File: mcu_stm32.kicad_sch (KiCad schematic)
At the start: 1 part, among them U1 STM32F103C6Tx

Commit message: stm32 added
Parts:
- removed U1: STM32F103C6Tx, Package_QFP:LQFP-48_7x7mm_P0.5mm, symbol MCU_ST_STM32F1:STM32F103C6Tx
- added C27, C28, C29, C30, C35: 0.1u, Capacitor_SMD:C_0805_2012Metric, symbol Device:C_Small
- added C31, C32, C33, C34: 20p, Capacitor_SMD:C_0805_2012Metric, symbol Device:C_Small
- added C36: 1uf, Capacitor_SMD:C_0805_2012Metric, symbol Device:C_Small
- added J16: Debug, Connector_PinHeader_2.54mm:PinHeader_1x04_P2.54mm_Vertical, symbol PCM_SL_Pin_Headers:PINHD_1x4_Male
- added J17: Boot_Sel, Connector_PinHeader_2.54mm:PinHeader_2x03_P2.54mm_Vertical, symbol PCM_SL_Pin_Headers:PINHD_2x3_Male
- added P1: USB_C_Plug_USB2.0, symbol Connector:USB_C_Plug_USB2.0
- added R16: 1M, Resistor_SMD:R_0805_2012Metric, symbol Device:R_Small
- added R17: 10K, Resistor_SMD:R_0805_2012Metric, symbol Device:R_Small
- added R18, R19: 100K, Resistor_SMD:R_0805_2012Metric, symbol Device:R_Small
- added R20, R21: 20R, Resistor_SMD:R_0805_2012Metric, symbol Device:R_Small
- added R22: 4.7K, Resistor_SMD:R_0805_2012Metric, symbol Device:R_Small
- added SW1: RESET, Button_Switch_SMD:SW_SPST_CK_KMS2xxGP, symbol Switch:SW_Push
- added U7: STM32F103C8Tx, Package_QFP:LQFP-48_7x7mm_P0.5mm, symbol MCU_ST_STM32F1:STM32F103C8Tx
- added Y1: 8mHz, symbol Device:Crystal_Small
- added Y2: 32.768kHz, symbol Device:Crystal_GND24_Small
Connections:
- new net: J17.3, R18.2
- new net: P1.A6 (D+), R21.1
- new net: J17.4, R19.1
- new net: P1.A7 (D-), R20.1
- new net 3V3: C27.2, C28.2, C29.2, C30.2, C35.2, J16.4, J17.1, J17.2, R17.1, U7.24 (VDD), U7.36 (VDD), U7.48 (VDD), U7.9 (VDDA)
- new net 5V1: P1.A4 (VBUS), P1.A9 (VBUS), P1.B4 (VBUS), P1.B9 (VBUS), R22.1
- new net BOOT0: R18.1, U7.44 (BOOT0)
- new net BOOT1: R19.2, U7.19 (PB1)
- new net GND: C27.1, C28.1, C29.1, C30.1, C31.2, C32.2, C33.2, C34.1, C35.1, C36.1, J16.1, J17.5, J17.6, P1.A1 (GND), P1.A12 (GND), P1.B1 (GND), P1.B12 (GND), P1.S1 (SHIELD), SW1.1, U7.23 (VSS), U7.35 (VSS), U7.47 (VSS), U7.8 (VSSA), Y2.2, Y2.4
- new net OSC_IN: C31.1, R16.1, U7.5 (PD0), Y1.2
- new net OSC_OUT: C32.1, R16.2, U7.6 (PD1), Y1.1
- new net PC14: C33.1, U7.3 (PC14), Y2.1
- new net PC15: C34.2, U7.4 (PC15), Y2.3
- new net RESET: C36.2, R17.2, SW1.2, U7.7 (NRST)
- new net SWCLK: J16.2
- new net SWDIO: J16.3
- new net USB_D+: R21.2, R22.2, U7.33 (PA12)
- new net USB_D-: R20.2, U7.32 (PA11)
- no-connect marks 0 -> 3

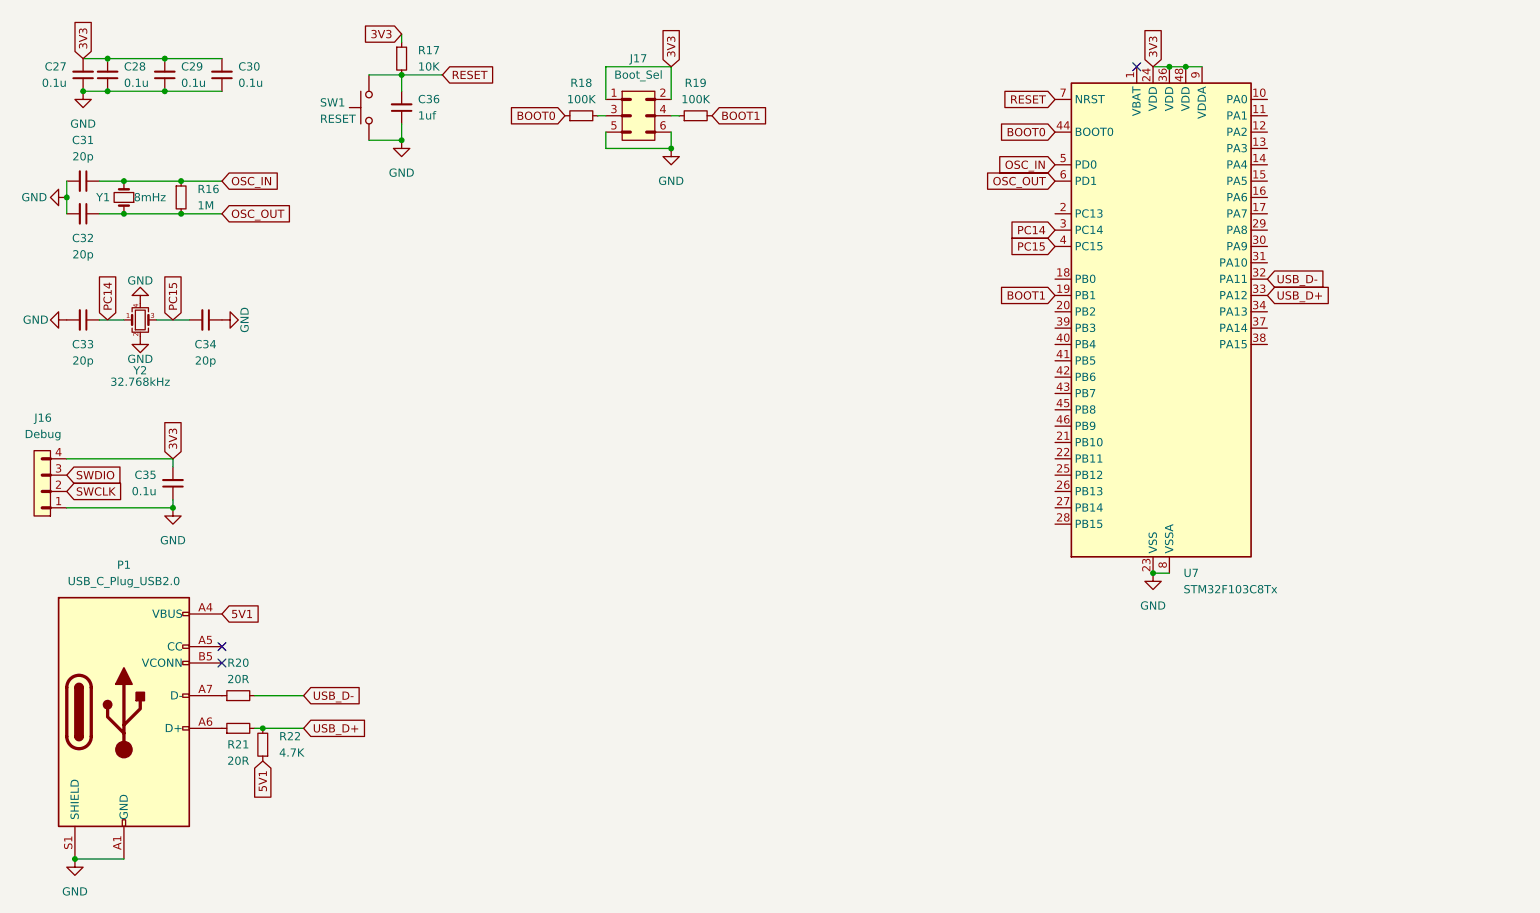
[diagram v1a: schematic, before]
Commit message: added components
servo controller, esp32
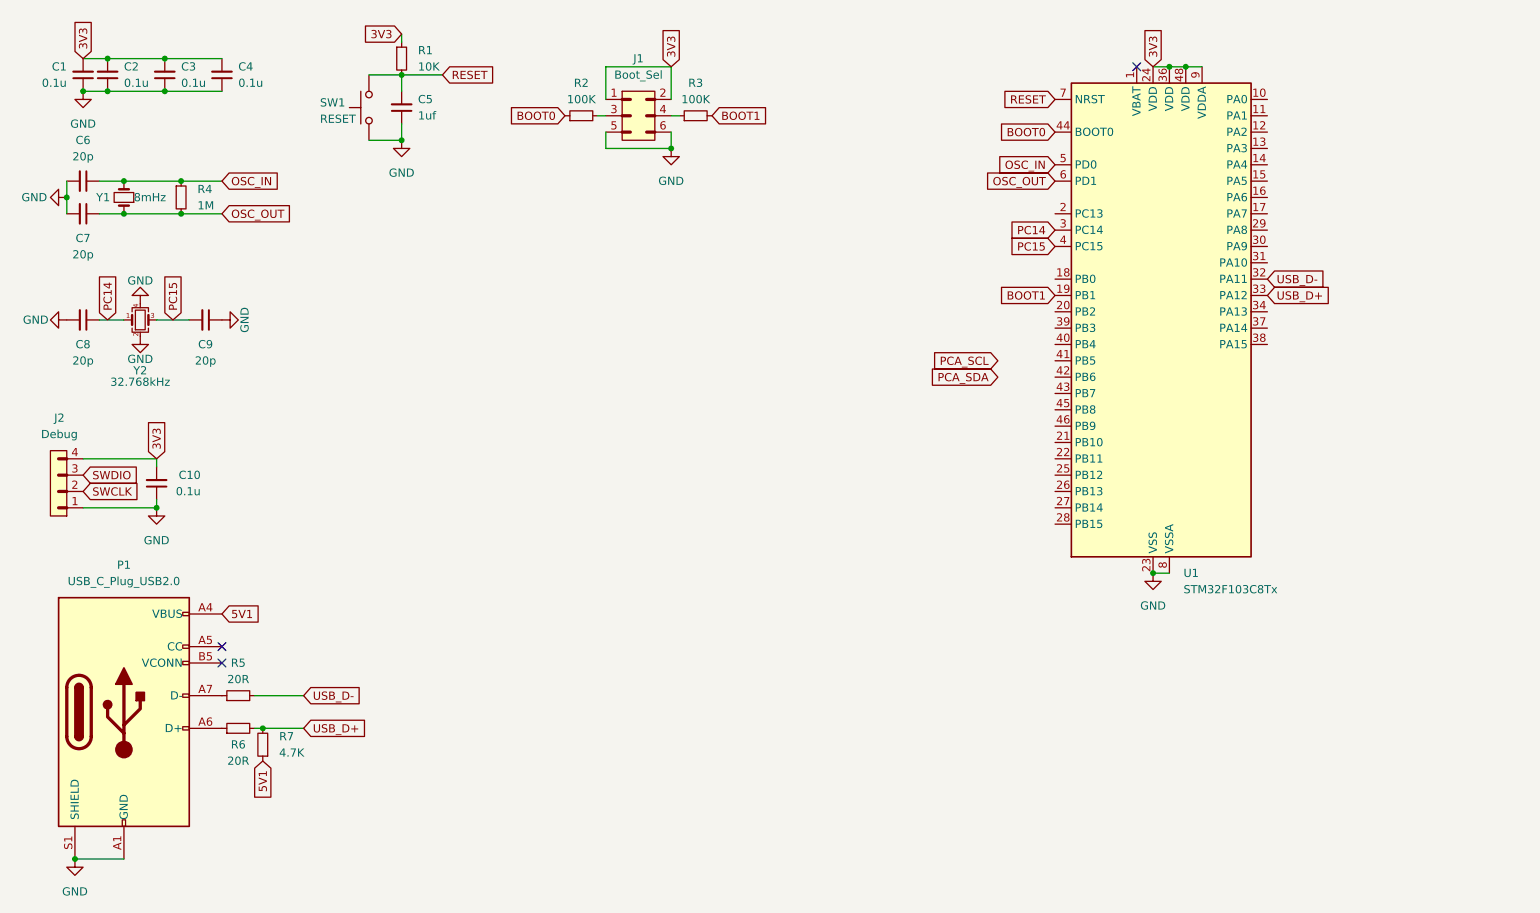
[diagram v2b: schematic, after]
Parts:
- renumbered C27 to C1, C35 to C10, C28 to C2, C29 to C3, C30 to C4, C36 to C5, C31 to C6, C32 to C7, C33 to C8, C34 to C9, J17 to J1, J16 to J2, R17 to R1, R18 to R2, R19 to R3, R16 to R4, R20 to R5, R21 to R6, R22 to R7, U7 to U1
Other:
- moved on the sheet: C10, J2

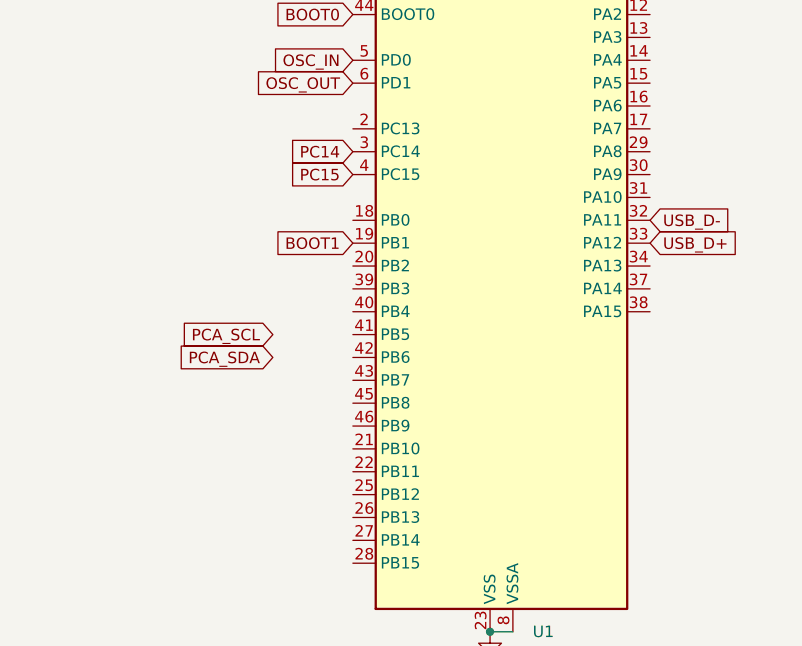
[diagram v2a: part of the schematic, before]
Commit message: some connectors added
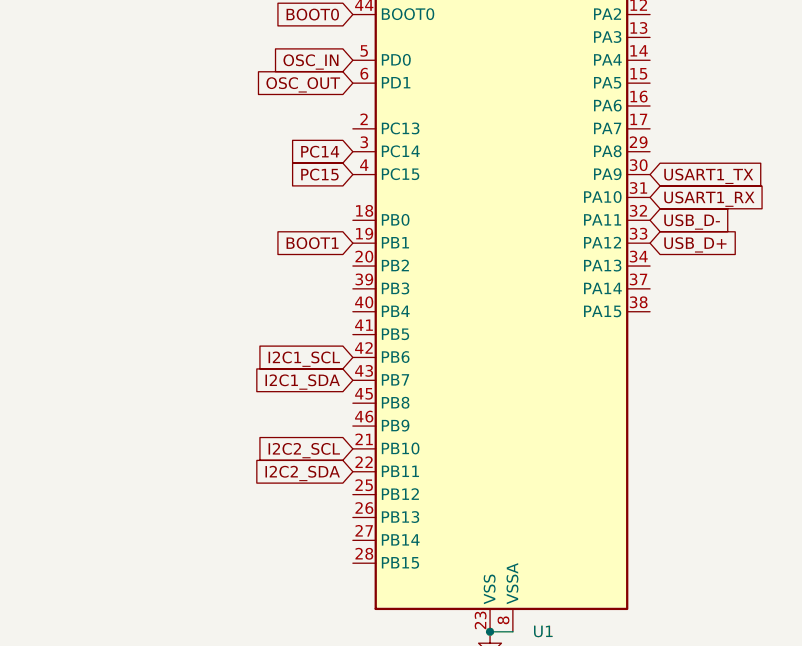
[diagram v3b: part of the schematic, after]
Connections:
- net I2C2_SCL: now reaches U1.21 (PB10)
- net I2C2_SDA: now reaches U1.22 (PB11)
- net USART1_TX: now reaches U1.30 (PA9)
- net USART1_RX: now reaches U1.31 (PA10)
- net I2C1_SCL: now reaches U1.42 (PB6)
- net I2C1_SDA: now reaches U1.43 (PB7)
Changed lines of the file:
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@@
+		)
+	)
+	(global_label "USART1_RX"
+		(shape input)
+		(at 207.01 50.8 0)
+		(fields_autoplaced yes)
+		(effects
+			(font
+				(size 1.27 1.27)
+			)
+			(justify left)
+		)
+		(property "Intersheetrefs" "${INTERSHEET_REFS}"
+			(at 220.518 50.8 0)
+			(effects
+				(font
+					(size 1.27 1.27)
+				)
+				(justify left)
+				(hide yes)
+			)
+		)
+	)
+	(global_label "USART1_TX"
+		(shape input)
+		(at 207.01 48.26 0)
+		(fields_autoplaced yes)
+		(effects
+			(font
+				(size 1.27 1.27)
+			)
+			(justify left)
+		)
+		(property "Intersheetrefs" "${INTERSHEET_REFS}"
+			(at 220.2156 48.26 0)
+			(effects
+				(font
+					(size 1.27 1.27)
+				)
+				(justify left)
+				(hide yes)
+			)
 		)
 	)
@@
 		)
 	)
-	(global_label "PCA_SCL"
-		(shape input)
-		(at 165.1 66.04 180)
-		(fields_autoplaced yes)
-		(effects
-			(font
-				(size 1.27 1.27)
-			)
-			(justify right)
-		)
-		(property "Intersheetrefs" "${INTERSHEET_REFS}"
-			(at 154.011 66.04 0)
-			(effects
-				(font
-					(size 1.27 1.27)
-				)
-				(justify right)
-				(hide yes)
-			)
-		)
-	)
-	(global_label "PCA_SDA"
-		(shape input)
-		(at 165.1 68.58 180)
-		(fields_autoplaced yes)
-		(effects
-			(font
-				(size 1.27 1.27)
-			)
-			(justify right)
-		)
-		(property "Intersheetrefs" "${INTERSHEET_REFS}"
-			(at 153.9505 68.58 0)
-			(effects
-				(font
-					(size 1.27 1.27)
-				)
-				(justify right)
-				(hide yes)
-			)
-		)
-	)
 	(global_label "OSC_OUT"
 		(shape input)
@@
 		)
 	)
+	(global_label "I2C2_SDA"
+		(shape input)
+		(at 173.99 81.28 180)
+		(fields_autoplaced yes)
+		(effects
+			(font
+				(size 1.27 1.27)
+			)
+			(justify right)
+		)
+		(property "Intersheetrefs" "${INTERSHEET_REFS}"
+			(at 162.1753 81.28 0)
+			(effects
+				(font
+					(size 1.27 1.27)
+				)
+				(justify right)
+				(hide yes)
+			)
+		)
+	)
 	(global_label "BOOT1"
 		(shape input)
@@
 				(hide yes)
 			)
+		)
+	)
+	(global_label "I2C2_SCL"
+		(shape input)
+		(at 173.99 78.74 180)
+		(fields_autoplaced yes)
+		(effects
+			(font
+				(size 1.27 1.27)
+			)
+			(justify right)
+		)
+		(property "Intersheetrefs" "${INTERSHEET_REFS}"
+			(at 162.2358 78.74 0)
+			(effects
+				(font
+					(size 1.27 1.27)
+				)
+				(justify right)
+				(hide yes)
+			)
+		)
+	)
+	(global_label "I2C1_SCL"
+		(shape input)
+		(at 173.99 68.58 180)
+		(fields_autoplaced yes)
+		(effects
+			(font
+				(size 1.27 1.27)
+			)
+			(justify right)
+		)
+		(property "Intersheetrefs" "${INTERSHEET_REFS}"
+			(at 162.2358 68.58 0)
+			(effects
+				(font
+					(size 1.27 1.27)
+				)
+				(justify right)
+				(hide yes)
+			)
+		)
+	)
+	(global_label "I2C1_SDA"
+		(shape input)
+		(at 173.99 71.12 180)
+		(fields_autoplaced yes)
+		(effects
+			(font
+				(size 1.27 1.27)
+			)
+			(justify right)
+		)
+		(property "Intersheetrefs" "${INTERSHEET_REFS}"
+			(at 162.1753 71.12 0)
+			(effects
+				(font
+					(size 1.27 1.27)
+				)
+				(justify right)
+				(hide yes)
+			)

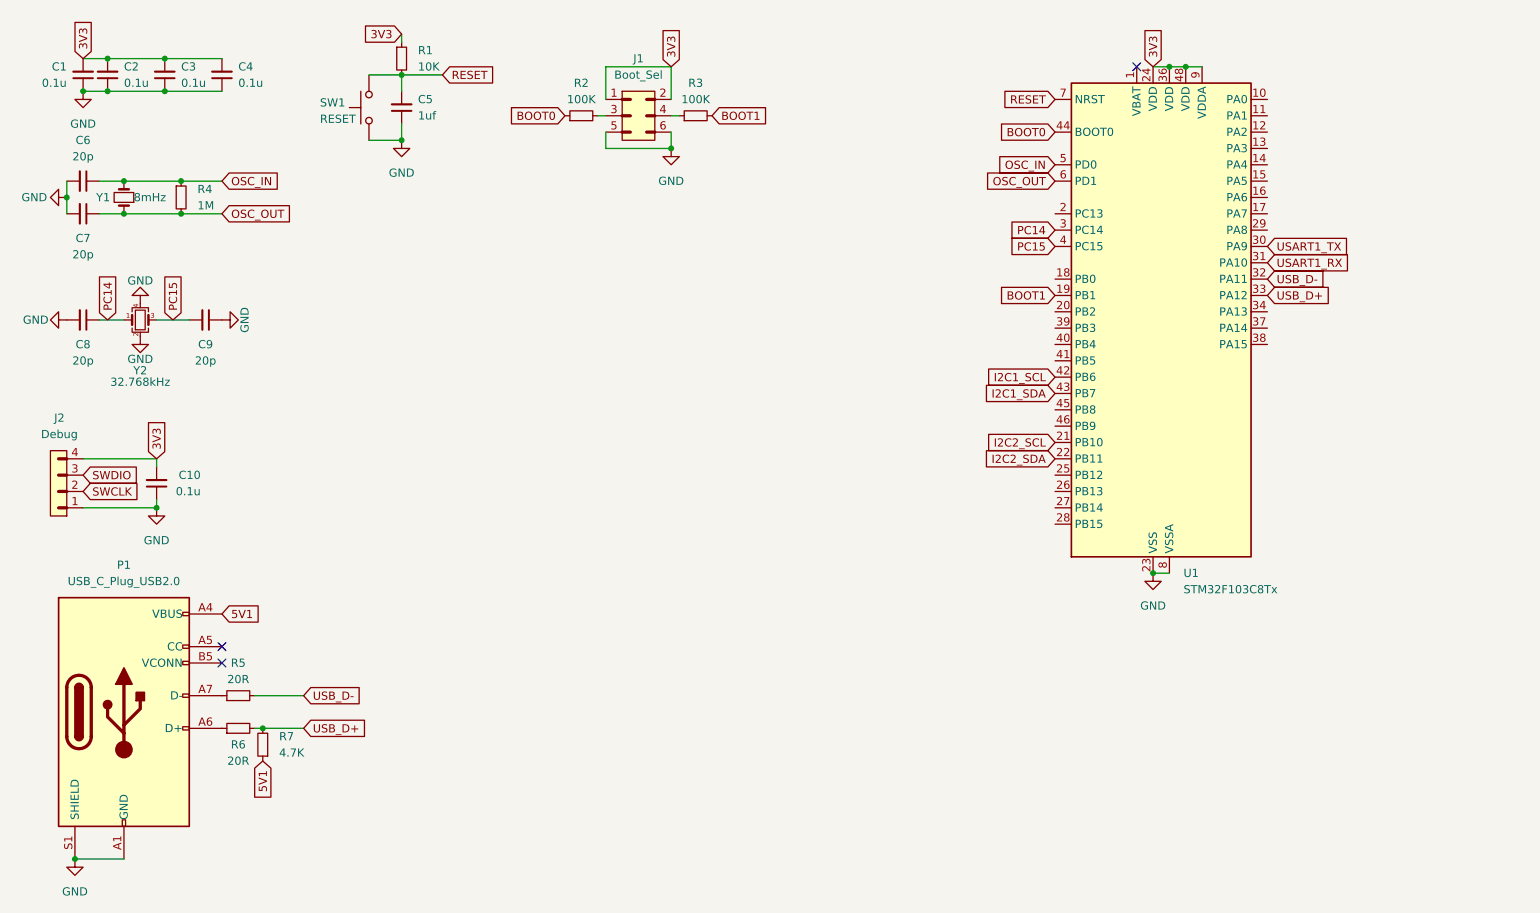
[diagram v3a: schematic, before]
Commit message: gpio expander added comm finished
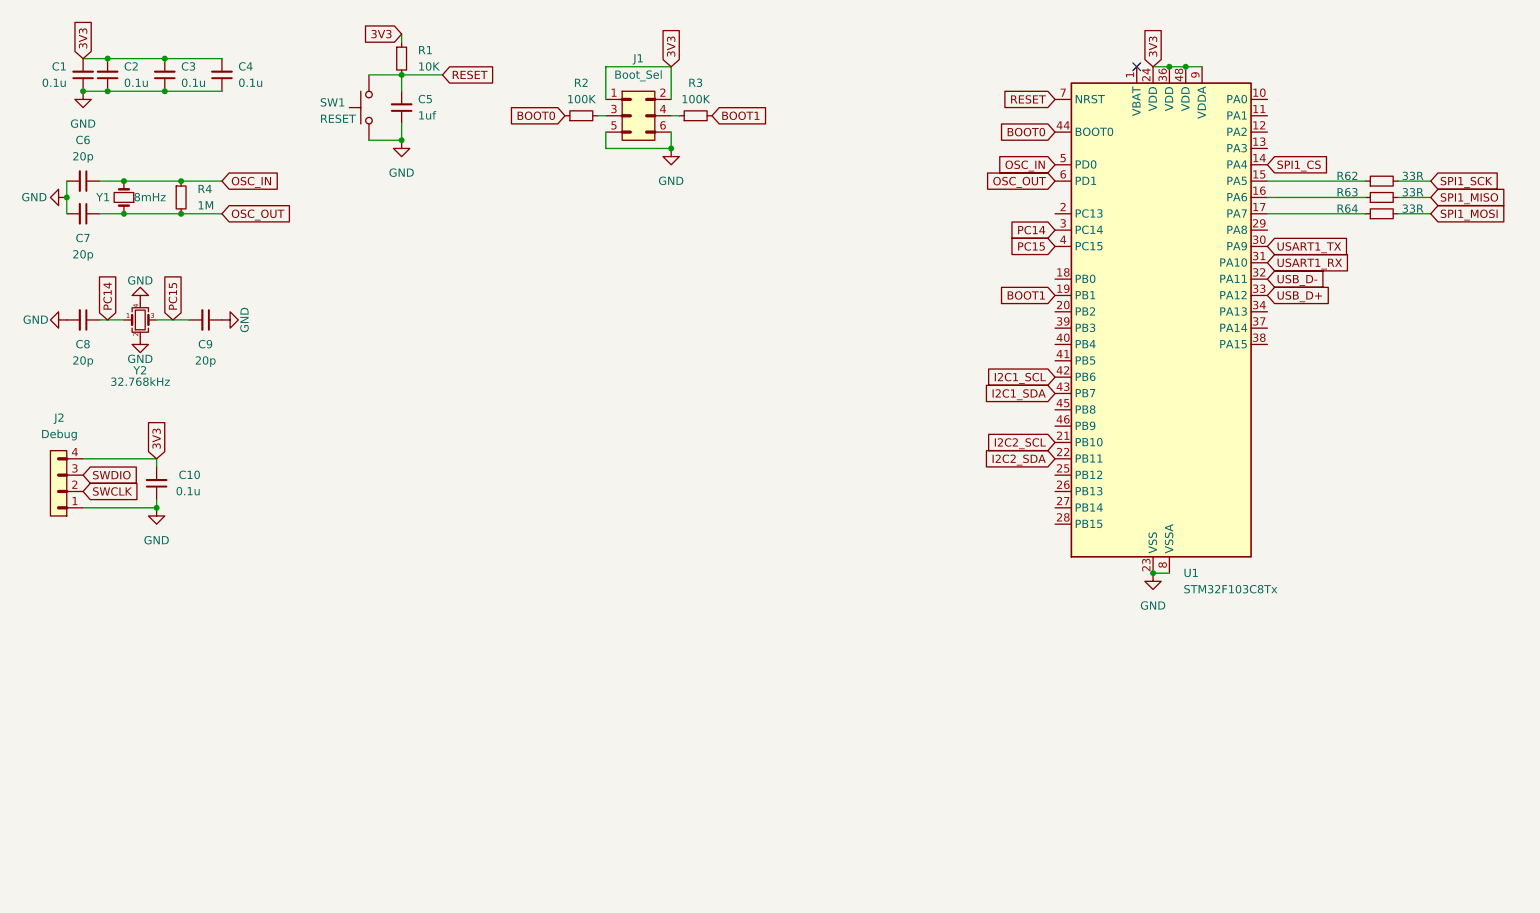
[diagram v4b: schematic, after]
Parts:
- removed P1: USB_C_Plug_USB2.0, symbol Connector:USB_C_Plug_USB2.0
- removed R5, R6: 20R, Resistor_SMD:R_0805_2012Metric, symbol Device:R_Small
- removed R7: 4.7K, Resistor_SMD:R_0805_2012Metric, symbol Device:R_Small
- added R62, R63, R64: 33R, Resistor_SMD:R_0805_2012Metric, symbol Device:R_Small
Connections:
- net SPI1_CS: now reaches U1.14 (PA4)
- net at U1.15 (PA5): now also R62.1
- net at U1.16 (PA6): now also R63.1
- net at U1.17 (PA7): now also R64.1
- new net SPI1_MISO: R63.2
- new net SPI1_MOSI: R64.2
- new net SPI1_SCK: R62.2
- no-connect marks 3 -> 1

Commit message: Visual Improvements
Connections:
- net SWCLK: now also U1.37 (PA14)
- net SWDIO: now also U1.34 (PA13)
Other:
- note added: "Boot Selection Headers"
- note added: "Clock"
- note added: "Debug pins for STLink"
- note added: "External Reset Button"
- note added: "STM32"
- note added: "STM32 Power Decoupling Caps"
- moved on the sheet: C1, C10, C2, C3, C4, C5, C6, C7, C8, C9, J1, J2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
